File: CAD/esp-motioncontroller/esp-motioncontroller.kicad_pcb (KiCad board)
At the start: 2 copper layers, 100 x 100 mm, 176 parts, among them J1 Conn_01x06, J2 Screw_Terminal_01x10, J3 Screw_Terminal_01x10, J4 Screw_Terminal_01x10, J6 Screw_Terminal_01x10, J7 Screw_Terminal_01x10, J8 Screw_Terminal_01x10, U1 ESP32-S3-DevKitC, U10 SP3485EN, U11 LTV-817S, U12 LTV-817S, U13 LTV-817S, U14 LTV-817S, U15 AMS1117-3.3, U16 SP3485EN, U17 SP3485EN, U18 SP3485EN, U19 SP3485EN, U2 SP3485EN, U20 SP3485EN, U21 SP3485EN, U22 SP3485EN, U23 SP3485EN, U24 SP3485EN, U3 XL1509-5.0E1, U4 SP3485EN, U5 SP3485EN, U6 LTV-817S, U7 LTV-817S, U8 LTV-817S, U9 LTV-817S

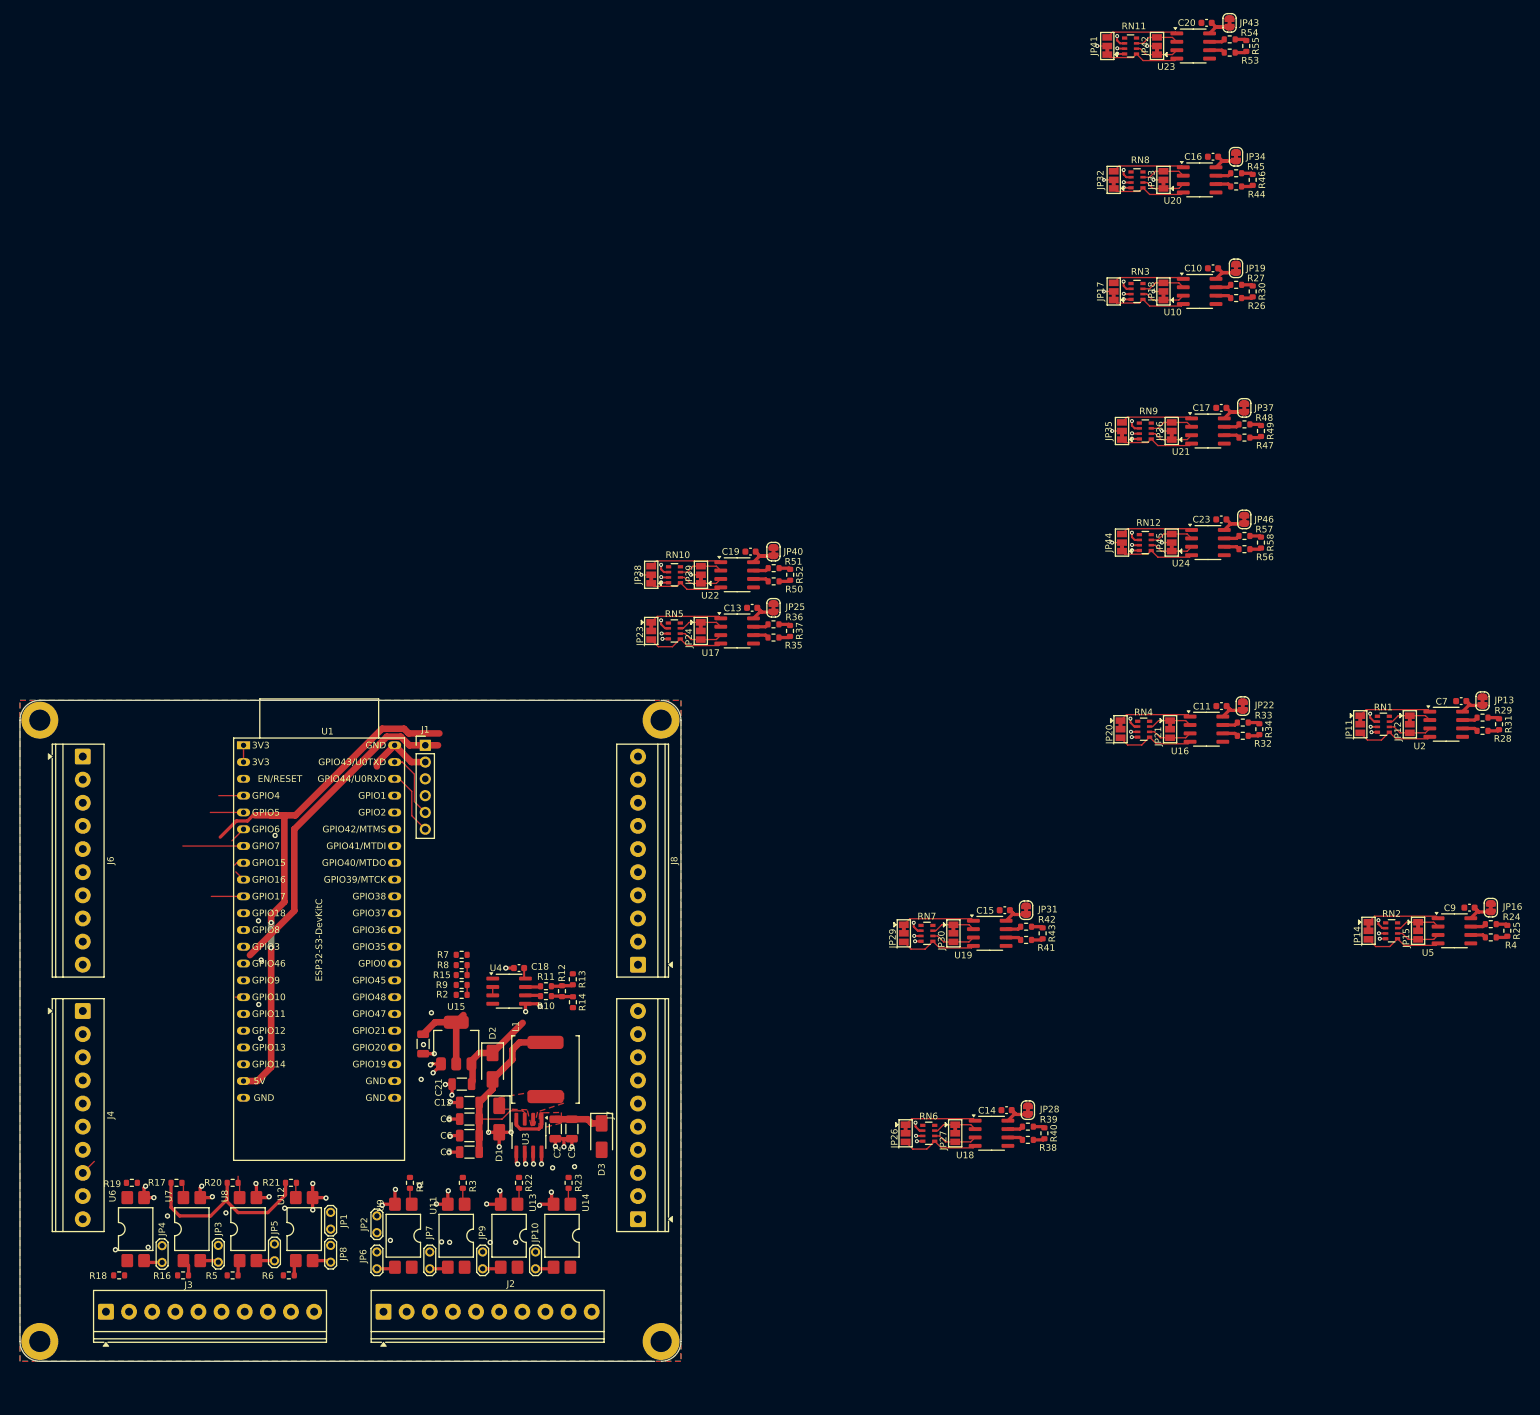
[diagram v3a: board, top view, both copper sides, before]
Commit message: Feat: Allmost complete sepdriver
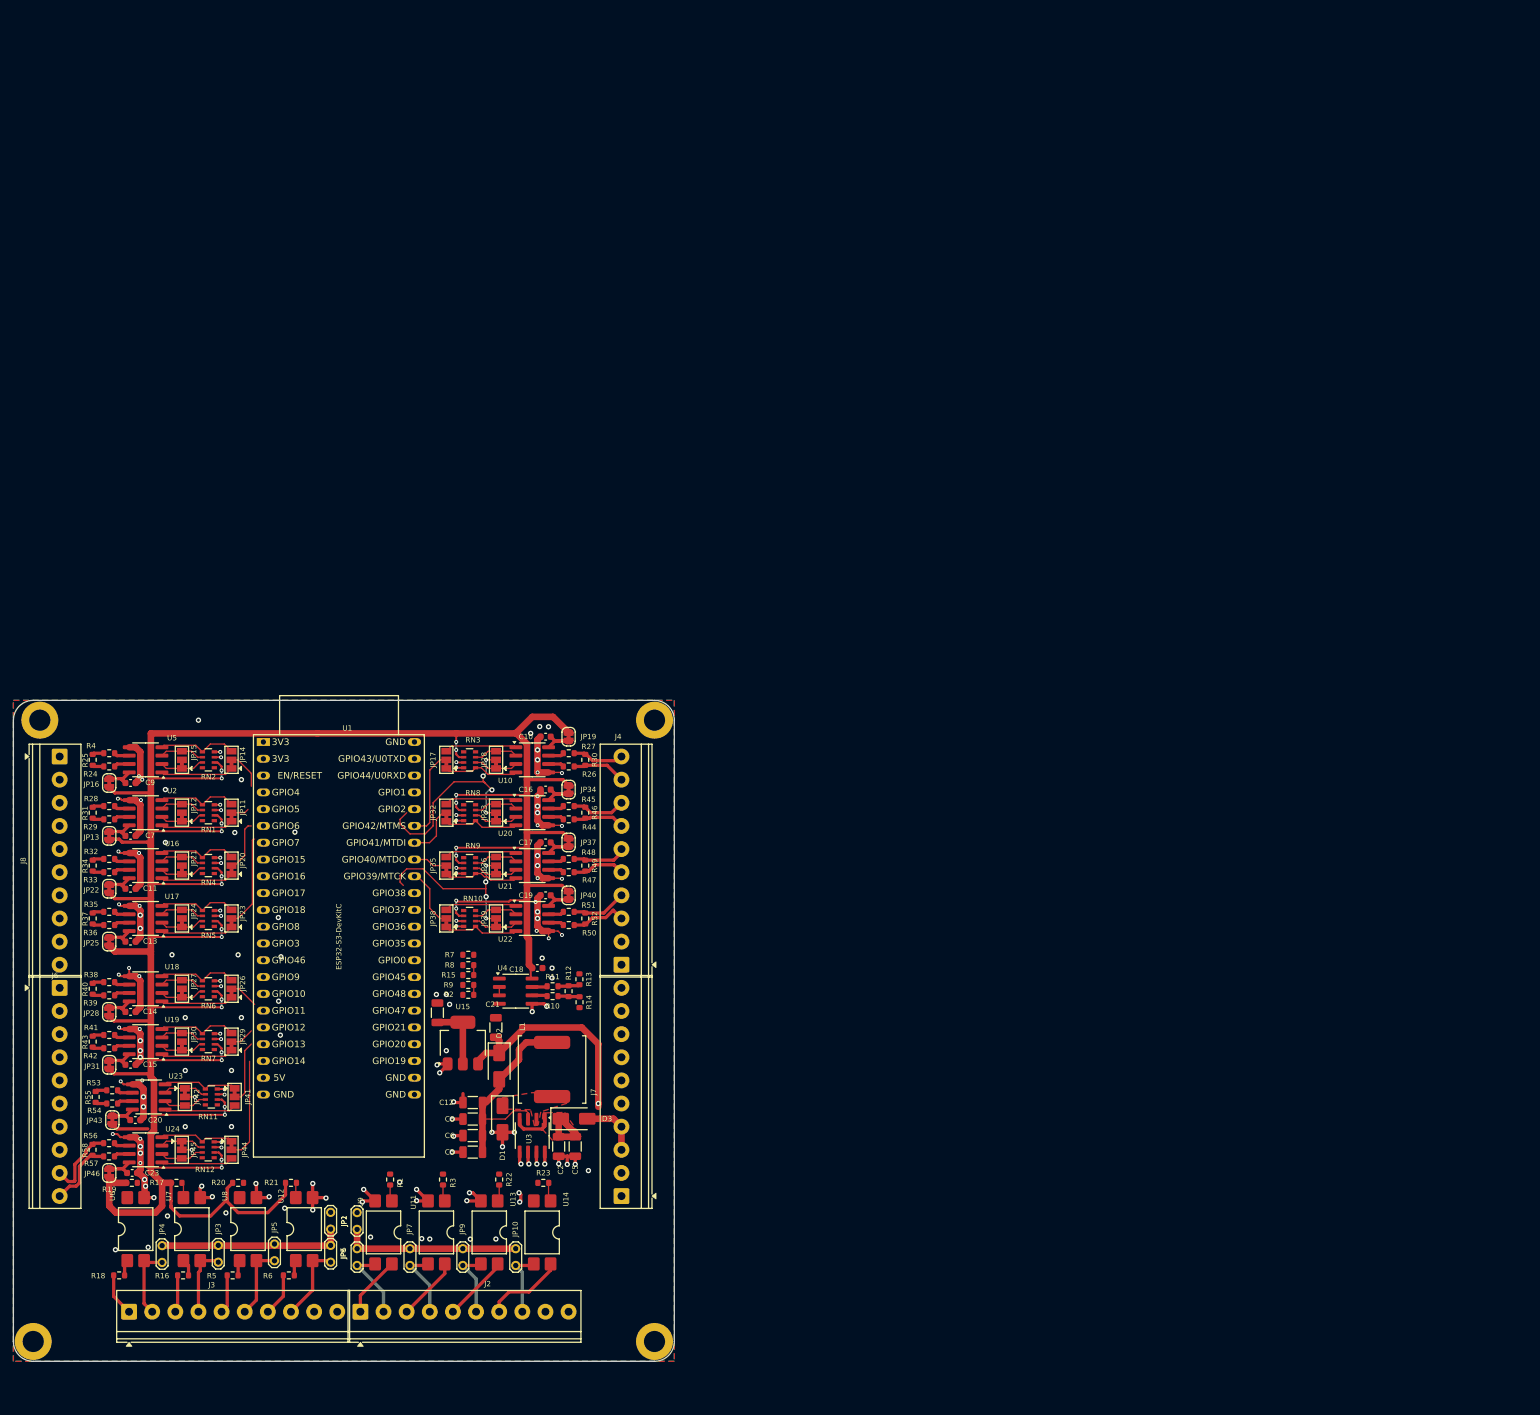
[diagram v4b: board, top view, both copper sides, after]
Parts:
- removed J1: Conn_01x06, Connector_PinHeader_2.54mm:PinHeader_1x06_P2.54mm_Vertical
- moved JP43 236.9 mm to (64.0, 107.5), turned to -90 degrees
- moved R55 235.8 mm to (61.5, 104.0), turned to 90 degrees
- moved R54 233.5 mm to (64.0, 105.0), turned to 180 degrees
- moved C20 232.0 mm to (67.5, 107.5), turned to 0 degrees
- moved R53 230.7 mm to (64.0, 103.0), turned to 180 degrees
- moved U23 224.2 mm to (69.5, 104.0), turned to 180 degrees
- moved JP42 216.6 mm to (75.0, 104.0), turned to -90 degrees
- moved R25 215.6 mm to (61.0, 53.0), turned to 90 degrees
- moved R31 213.2 mm to (61.0, 61.0), turned to 90 degrees
- moved RN11 211.2 mm to (79.0, 104.0), turned to 0 degrees
- moved R4 210.9 mm to (63.5, 52.0), turned to 180 degrees
- moved R24 210.4 mm to (63.5, 54.0), turned to 180 degrees
- moved JP16 209.9 mm to (63.5, 56.5), turned to -90 degrees
- moved JP13 208.8 mm to (63.5, 64.5), turned to -90 degrees
- moved R29 208.3 mm to (63.5, 62.0), turned to 180 degrees
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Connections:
- J4 pad 10: unconnected-(J4-Pin_10-Pad10) -> /InputOutput/DIFF_OUTPUT1/IOP
- J4 pad 3: unconnected-(J4-Pin_3-Pad3) -> /InputOutput/DIFF_OUTPUT4/ION
- J4 pad 4: unconnected-(J4-Pin_4-Pad4) -> /InputOutput/DIFF_OUTPUT4/IOP
- J4 pad 5: unconnected-(J4-Pin_5-Pad5) -> /InputOutput/DIFF_OUTPUT3/ION
- J4 pad 6: unconnected-(J4-Pin_6-Pad6) -> /InputOutput/DIFF_OUTPUT3/IOP
- J4 pad 7: unconnected-(J4-Pin_7-Pad7) -> /InputOutput/DIFF_OUTPUT2/ION
- J4 pad 8: unconnected-(J4-Pin_8-Pad8) -> /InputOutput/DIFF_OUTPUT2/IOP
- J4 pad 9: unconnected-(J4-Pin_9-Pad9) -> /InputOutput/DIFF_OUTPUT1/ION
- J6 pad 10: unconnected-(J6-Pin_10-Pad10) -> /InputOutput/DIFF_OUTPUT6/IOP
- J6 pad 7: unconnected-(J6-Pin_7-Pad7) -> /InputOutput/DIFF_OUTPUT5/ION
- J6 pad 8: unconnected-(J6-Pin_8-Pad8) -> /InputOutput/DIFF_OUTPUT5/IOP
- J6 pad 9: unconnected-(J6-Pin_9-Pad9) -> /InputOutput/DIFF_OUTPUT6/ION
- JP17 pad 2: /InputOutput/DIFF_OUTPUT1/IO -> /InputOutput/HIO1
- JP32 pad 2: /InputOutput/DIFF_OUTPUT2/IO -> /InputOutput/HIO2
- JP33 pad 2: /InputOutput/DIFF_OUTPUT2/ENBL -> /InputOutput/DIFF_OUTPUT1/ENBL
- JP35 pad 2: /InputOutput/DIFF_OUTPUT3/IO -> /InputOutput/HIO3
- JP38 pad 2: /InputOutput/DIFF_OUTPUT4/IO -> /InputOutput/HIO4
- JP39 pad 2: /InputOutput/DIFF_OUTPUT4/ENBL -> /InputOutput/DIFF_OUTPUT3/ENBL
- R24 pad 2: /InputOutput/DIFF_INPUT1/ION -> /InputOutput/DIFF_INPUT1/IOP
- R25 pad 1: /InputOutput/DIFF_INPUT1/ION -> /InputOutput/DIFF_INPUT1/IOP
- R25 pad 2: /InputOutput/DIFF_INPUT1/IOP -> /InputOutput/DIFF_INPUT1/ION
- R26 pad 2: /InputOutput/DIFF_OUTPUT1/IOP -> /InputOutput/DIFF_OUTPUT1/ION
- R27 pad 2: /InputOutput/DIFF_OUTPUT1/ION -> /InputOutput/DIFF_OUTPUT1/IOP
- R28 pad 2: /InputOutput/DIFF_INPUT2/IOP -> /InputOutput/DIFF_INPUT2/ION
- R29 pad 2: /InputOutput/DIFF_INPUT2/ION -> /InputOutput/DIFF_INPUT2/IOP
- R30 pad 1: /InputOutput/DIFF_OUTPUT1/ION -> /InputOutput/DIFF_OUTPUT1/IOP
- R30 pad 2: /InputOutput/DIFF_OUTPUT1/IOP -> /InputOutput/DIFF_OUTPUT1/ION
- R31 pad 1: /InputOutput/DIFF_INPUT2/ION -> /InputOutput/DIFF_INPUT2/IOP
- R31 pad 2: /InputOutput/DIFF_INPUT2/IOP -> /InputOutput/DIFF_INPUT2/ION
- R32 pad 2: /InputOutput/DIFF_INPUT3/IOP -> /InputOutput/DIFF_INPUT3/ION
- R33 pad 2: /InputOutput/DIFF_INPUT3/ION -> /InputOutput/DIFF_INPUT3/IOP
- R34 pad 1: /InputOutput/DIFF_INPUT3/ION -> /InputOutput/DIFF_INPUT3/IOP
- R34 pad 2: /InputOutput/DIFF_INPUT3/IOP -> /InputOutput/DIFF_INPUT3/ION
- R35 pad 2: /InputOutput/DIFF_INPUT4/IOP -> /InputOutput/DIFF_INPUT4/ION
- R36 pad 2: /InputOutput/DIFF_INPUT4/ION -> /InputOutput/DIFF_INPUT4/IOP
- R37 pad 1: /InputOutput/DIFF_INPUT4/ION -> /InputOutput/DIFF_INPUT4/IOP
- R37 pad 2: /InputOutput/DIFF_INPUT4/IOP -> /InputOutput/DIFF_INPUT4/ION
- R38 pad 2: /InputOutput/DIFF_INPUT5/IOP -> /InputOutput/DIFF_INPUT5/ION
- R39 pad 2: /InputOutput/DIFF_INPUT5/ION -> /InputOutput/DIFF_INPUT5/IOP
- R4 pad 2: /InputOutput/DIFF_INPUT1/IOP -> /InputOutput/DIFF_INPUT1/ION
- R40 pad 1: /InputOutput/DIFF_INPUT5/ION -> /InputOutput/DIFF_INPUT5/IOP
- R40 pad 2: /InputOutput/DIFF_INPUT5/IOP -> /InputOutput/DIFF_INPUT5/ION
- R41 pad 2: /InputOutput/DIFF_INPUT6/IOP -> /InputOutput/DIFF_INPUT6/ION
- R42 pad 2: /InputOutput/DIFF_INPUT6/ION -> /InputOutput/DIFF_INPUT6/IOP
- R43 pad 1: /InputOutput/DIFF_INPUT6/ION -> /InputOutput/DIFF_INPUT6/IOP
- R43 pad 2: /InputOutput/DIFF_INPUT6/IOP -> /InputOutput/DIFF_INPUT6/ION
- R44 pad 2: /InputOutput/DIFF_OUTPUT2/IOP -> /InputOutput/DIFF_OUTPUT2/ION
- R45 pad 2: /InputOutput/DIFF_OUTPUT2/ION -> /InputOutput/DIFF_OUTPUT2/IOP
- R46 pad 1: /InputOutput/DIFF_OUTPUT2/ION -> /InputOutput/DIFF_OUTPUT2/IOP
- R46 pad 2: /InputOutput/DIFF_OUTPUT2/IOP -> /InputOutput/DIFF_OUTPUT2/ION
- R47 pad 2: /InputOutput/DIFF_OUTPUT3/IOP -> /InputOutput/DIFF_OUTPUT3/ION
- R48 pad 2: /InputOutput/DIFF_OUTPUT3/ION -> /InputOutput/DIFF_OUTPUT3/IOP
- R49 pad 1: /InputOutput/DIFF_OUTPUT3/ION -> /InputOutput/DIFF_OUTPUT3/IOP
- R49 pad 2: /InputOutput/DIFF_OUTPUT3/IOP -> /InputOutput/DIFF_OUTPUT3/ION
- R50 pad 2: /InputOutput/DIFF_OUTPUT4/IOP -> /InputOutput/DIFF_OUTPUT4/ION
- R51 pad 2: /InputOutput/DIFF_OUTPUT4/ION -> /InputOutput/DIFF_OUTPUT4/IOP
- R52 pad 1: /InputOutput/DIFF_OUTPUT4/ION -> /InputOutput/DIFF_OUTPUT4/IOP
- R52 pad 2: /InputOutput/DIFF_OUTPUT4/IOP -> /InputOutput/DIFF_OUTPUT4/ION
- R53 pad 2: /InputOutput/DIFF_OUTPUT5/IOP -> /InputOutput/DIFF_OUTPUT5/ION
- R54 pad 2: /InputOutput/DIFF_OUTPUT5/ION -> /InputOutput/DIFF_OUTPUT5/IOP
- R55 pad 1: /InputOutput/DIFF_OUTPUT5/ION -> /InputOutput/DIFF_OUTPUT5/IOP
- R55 pad 2: /InputOutput/DIFF_OUTPUT5/IOP -> /InputOutput/DIFF_OUTPUT5/ION
- R56 pad 2: /InputOutput/DIFF_OUTPUT6/IOP -> /InputOutput/DIFF_OUTPUT6/ION
- R57 pad 2: /InputOutput/DIFF_OUTPUT6/ION -> /InputOutput/DIFF_OUTPUT6/IOP
- R58 pad 1: /InputOutput/DIFF_OUTPUT6/ION -> /InputOutput/DIFF_OUTPUT6/IOP
- R58 pad 2: /InputOutput/DIFF_OUTPUT6/IOP -> /InputOutput/DIFF_OUTPUT6/ION
- U1 pad 10: /esp32-s3/ENBL_HO -> unconnected-(U1-GPIO17/ADC2_CH6-Pad10)
- U1 pad 30: /InputOutput/RE/DE -> unconnected-(U1-GPIO45-Pad30)
- U1 pad 36: unconnected-(U1-GPIO39/MTCK-Pad36) -> /InputOutput/HIO4
- U1 pad 37: unconnected-(U1-GPIO40/MTDO-Pad37) -> /InputOutput/HIO3
- U1 pad 38: unconnected-(U1-GPIO41/MTDI-Pad38) -> /InputOutput/HIO2
- U1 pad 39: unconnected-(U1-GPIO42/MTMS-Pad39) -> /InputOutput/HIO1
- U1 pad 4: /esp32-s3/HO4 -> unconnected-(U1-GPIO4/ADC1_CH3-Pad4)
- U1 pad 40: /InputOutput/TXD -> unconnected-(U1-GPIO2/ADC1_CH1-Pad40)
- U1 pad 41: /InputOutput/RXD -> unconnected-(U1-GPIO1/ADC1_CH0-Pad41)
- U1 pad 42: /esp32-s3/rx -> unconnected-(U1-GPIO44/U0RXD-Pad42)
- U1 pad 43: /esp32-s3/tx -> unconnected-(U1-GPIO43/U0TXD-Pad43)
- U1 pad 5: /esp32-s3/HO3 -> unconnected-(U1-GPIO5/ADC1_CH4-Pad5)
- U1 pad 6: /esp32-s3/HO2 -> unconnected-(U1-GPIO6/ADC1_CH5-Pad6)
- U1 pad 7: /esp32-s3/HO1 -> unconnected-(U1-GPIO7/ADC1_CH6-Pad7)
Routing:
- net +3.3V: track 117.9 -> 459.3 mm, vias 12 -> 24
- net GND: track 106.4 -> 222.8 mm, vias 84 -> 146
- net 5V: track 98.6 -> 33.6 mm, vias 2 -> 1
- net /InputOutput/DIFF_OUTPUT1/ENBL: track 1.50 -> 33.4 mm, vias 1 -> 4
- net GND_OPTO_OUT: track 0.00 -> 28.0 mm
- net GND_OPTO_IN: track 0.00 -> 26.9 mm
- net /InputOutput/DIFF_OUTPUT3/ENBL: track 1.50 -> 27.4 mm, vias 1 -> 4
- net /InputOutput/DIFF_INPUT4/IO: track 0.00 -> 14.1 mm
- net /InputOutput/DIFF_OUTPUT6/IO: track 1.50 -> 15.4 mm, vias 1 -> 0
- net /InputOutput/HIO1: track 0.00 -> 13.6 mm
- net /InputOutput/OPTO_OUT_4: track 0.00 -> 12.2 mm
- net /esp32-s3/tx: track 10.2 -> 0.00 mm
- net /InputOutput/OPTO_OUT_3: track 0.00 -> 10.0 mm
- net /InputOutput/OPTO_OUT_2: track 0.00 -> 9.63 mm
- net /InputOutput/DIFF_OUTPUT6/ION: track 1.75 -> 11.3 mm
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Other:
- outline, holes or cut-outs redrawn
